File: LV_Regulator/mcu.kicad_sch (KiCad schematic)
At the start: 20 parts, among them U4 STM32F103C8Tx, Y1 32.768kHz, Y2 8MHz

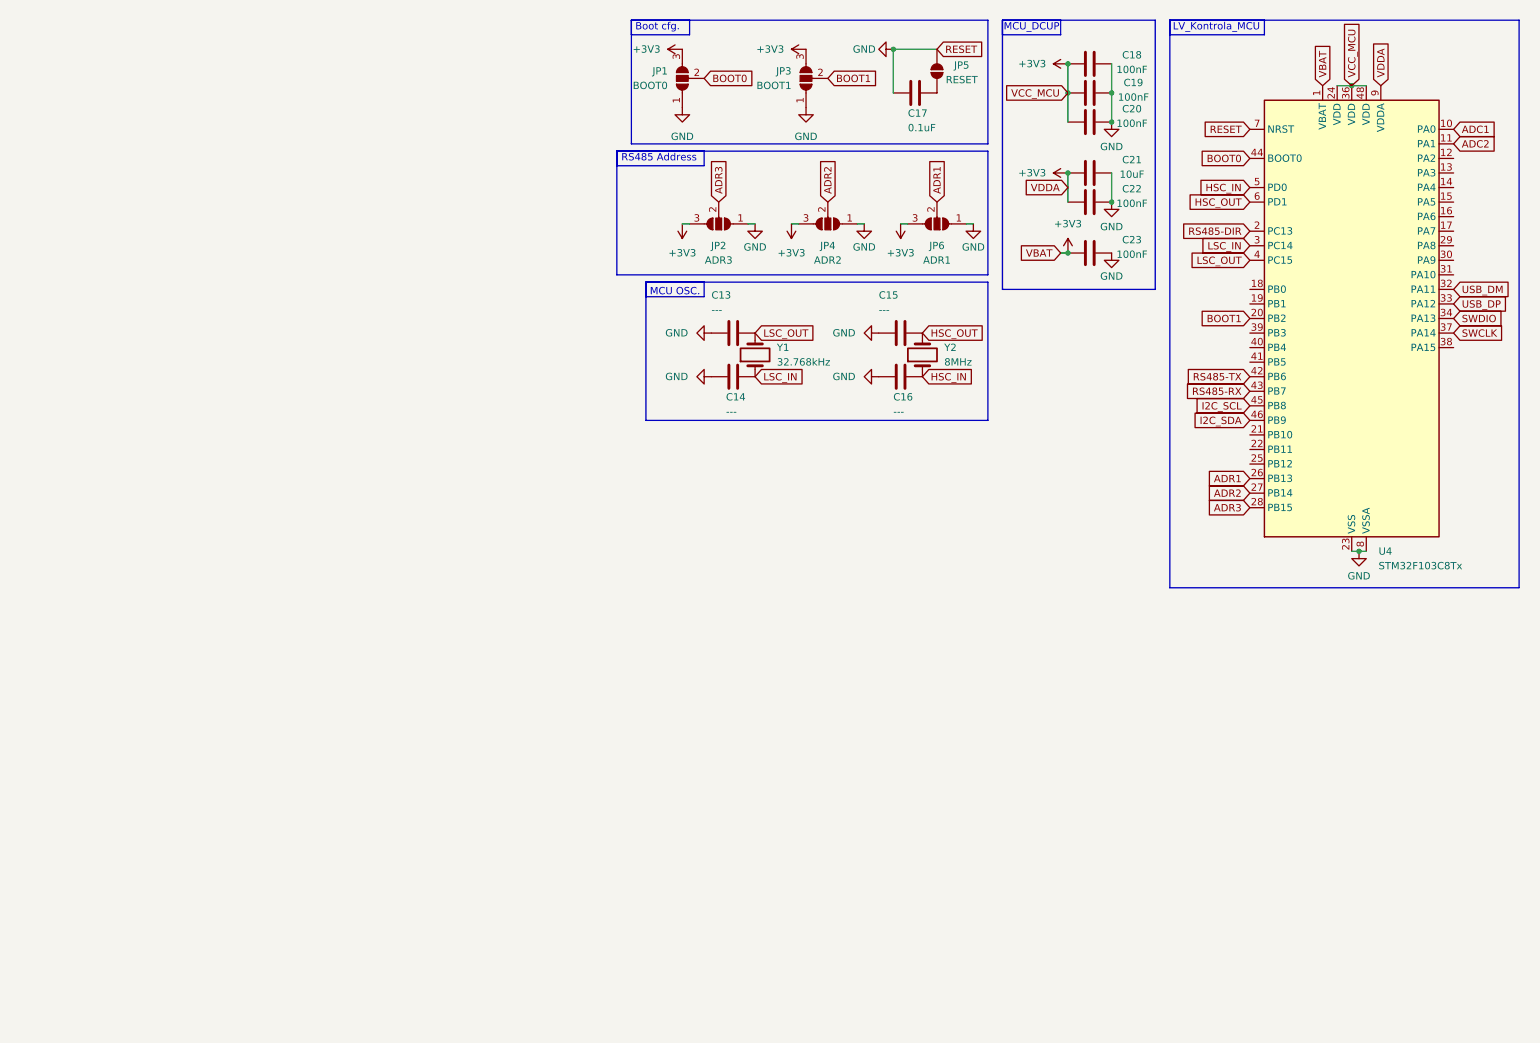
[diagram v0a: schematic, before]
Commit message: LV_Regulator Control changes
Added debug and development equipment, added config. eeprom, more...
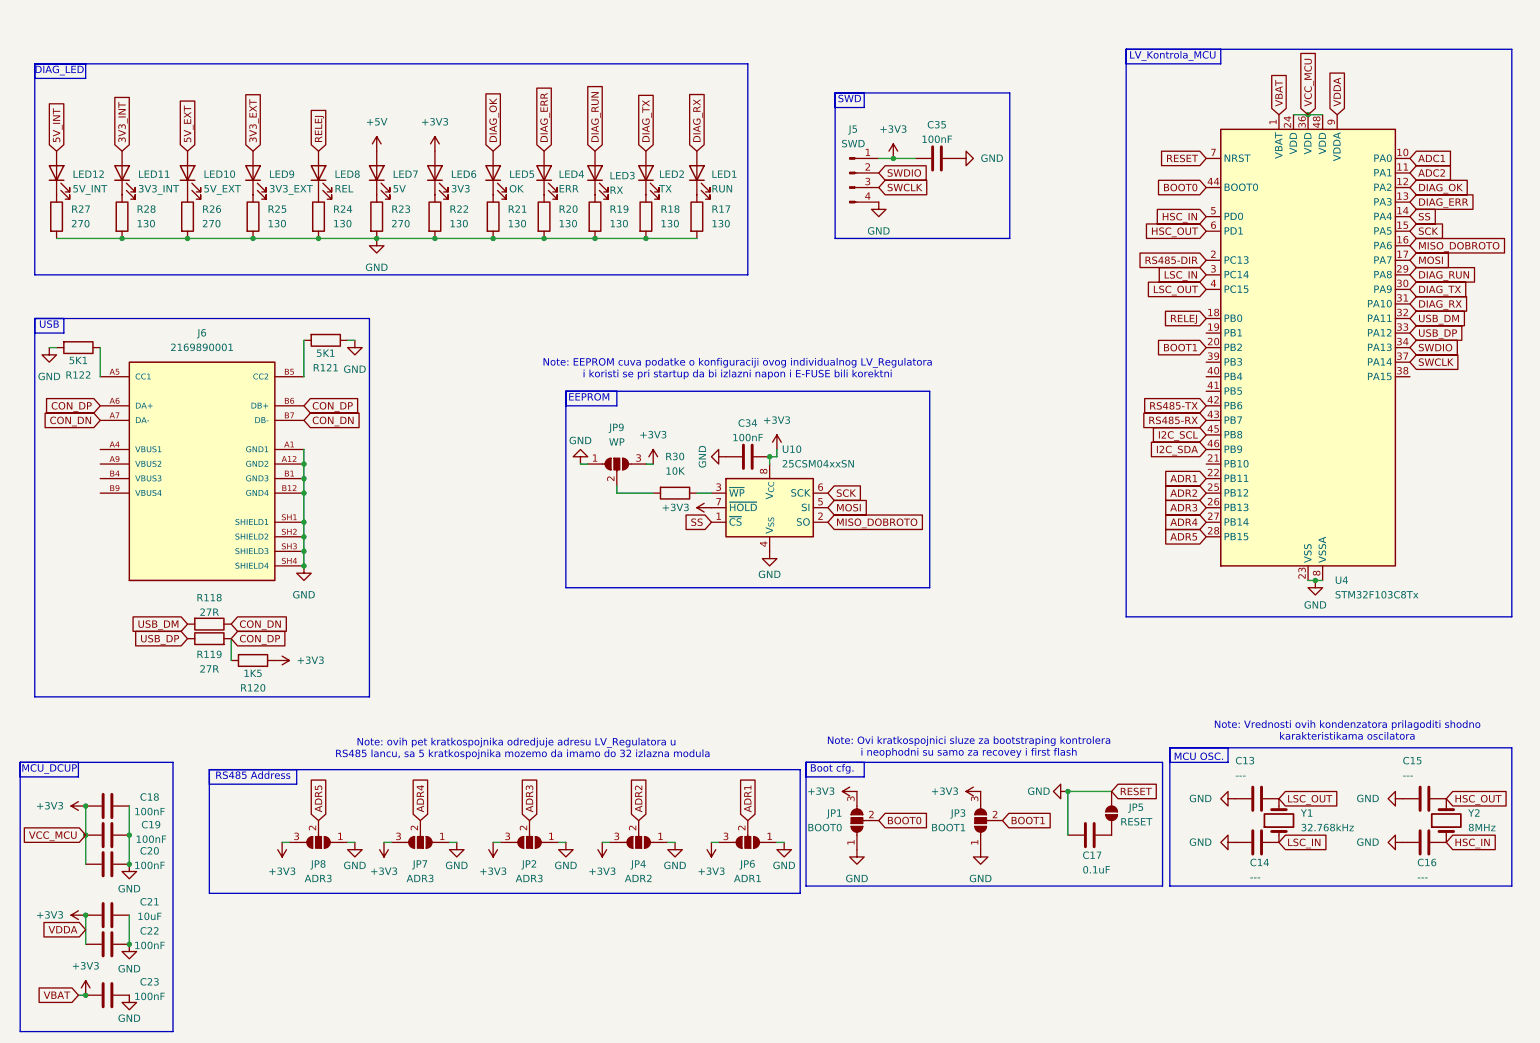
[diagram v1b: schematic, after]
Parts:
- added C34, C35: 100nF, symbol Device:C
- added J5: SWD, symbol Connector:Conn_01x04_Pin
- added J6: 2169890001, USB-C:MOLEX_2169890001, symbol 2169890001:2169890001
- added JP7, JP8: ADR3, symbol Jumper:SolderJumper_3_Open
- added JP9: WP, symbol Jumper:SolderJumper_3_Open
- added LED1: RUN, symbol Device:LED
- added LED10: 5V_EXT, symbol Device:LED
- added LED11: 3V3_INT, symbol Device:LED
- added LED12: 5V_INT, symbol Device:LED
- added LED2: TX, symbol Device:LED
- added LED3: RX, symbol Device:LED
- added LED4: ERR, symbol Device:LED
- added LED5: OK, symbol Device:LED
- added LED6: 3V3, symbol Device:LED
- added LED7: 5V, symbol Device:LED
- added LED8: REL, symbol Device:LED
- added LED9: 3V3_EXT, symbol Device:LED
- added R118, R119: 27R, Resistor_SMD:R_1206_3216Metric_Pad1.30x1.75mm_HandSolder, symbol Device:R
- added R120: 1K5, Resistor_SMD:R_1206_3216Metric_Pad1.30x1.75mm_HandSolder, symbol Device:R
- added R121, R122: 5K1, Resistor_SMD:R_1206_3216Metric_Pad1.30x1.75mm_HandSolder, symbol Device:R
- added R17, R18, R19, R20, R21, R22, R24, R25, R28: 130, symbol Device:R
- added R23, R26, R27: 270, symbol Device:R
- added R30: 10K, symbol Device:R
- added U10: 25CSM04xxSN, Package_SO:SOIC-8_3.9x4.9mm_P1.27mm, symbol Memory_EEPROM:25CSM04xxSN
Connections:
- net +3V3: now also C34.1, C35.2, J5.1 (Pin_1), JP7.3 (B), JP8.3 (B), JP9.3 (B), LED6.2 (A), R120.1, U10.7 (~{HOLD}), U10.8 (V_{CC})
- net ADR1: now also U4.22 (PB11); no longer U4.26 (PB13)
- net ADR2: now also U4.25 (PB12); no longer U4.27 (PB14)
- net ADR3: now also U4.26 (PB13); no longer U4.28 (PB15)
- net GND: now also C34.2, C35.1, J5.4 (Pin_4), J6.A1 (GND1), J6.A12 (GND2), J6.B1 (GND3), J6.B12 (GND4), J6.SH1 (SHIELD1), J6.SH2 (SHIELD2), J6.SH3 (SHIELD3), J6.SH4 (SHIELD4), JP7.1 (A), JP8.1 (A), JP9.1 (A), R121.1, R122.2, R17.2, R18.2, R19.2, R20.2, R21.2, R22.2, R23.2, R24.2, R25.2, R26.2, R27.2, R28.2, U10.4 (V_{SS})
- net SWCLK: now also J5.3 (Pin_3)
- net SWDIO: now also J5.2 (Pin_2)
- net USB_DM: now also R118.2
- net USB_DP: now also R119.1
- net DIAG_OK: now reaches U4.12 (PA2)
- net DIAG_OK: now also LED5.2 (A)
- net DIAG_ERR: now reaches U4.13 (PA3)
- net DIAG_ERR: now also LED4.2 (A)
- net SS: now reaches U4.14 (PA4)
- net SS: now also U10.1 (~{CS})
- net SCK: now reaches U4.15 (PA5)
- net SCK: now also U10.6 (SCK)
- net MISO_DOBROTO: now reaches U4.16 (PA6)
- net MISO_DOBROTO: now also U10.2 (SO)
- net MOSI: now reaches U4.17 (PA7)
- net MOSI: now also U10.5 (SI)
- net RELEJ: now reaches U4.18 (PB0)
- net RELEJ: now also LED8.2 (A)
- net DIAG_RUN: now reaches U4.29 (PA8)
- net DIAG_RUN: now also LED3.2 (A)
- net DIAG_TX: now reaches U4.30 (PA9)
- net DIAG_TX: now also LED2.2 (A)
- net DIAG_RX: now reaches U4.31 (PA10)
- net DIAG_RX: now also LED1.2 (A)
- new net: LED7.1 (K), R23.1
- new net: R30.1, U10.3 (~{WP})
- new net: J6.A5 (CC1), R122.1
- new net: J6.B5 (CC2), R121.2
- new net: LED6.1 (K), R22.1
- new net: LED2.1 (K), R18.1
- new net: JP9.2 (C), R30.2
- new net: LED12.1 (K), R27.1
- new net: LED4.1 (K), R20.1
- new net: LED9.1 (K), R25.1
- new net: LED11.1 (K), R28.1
- new net: LED1.1 (K), R17.1
- new net: LED5.1 (K), R21.1
- new net: LED10.1 (K), R26.1
- new net: LED3.1 (K), R19.1
- new net: LED8.1 (K), R24.1
- new net +5V: LED7.2 (A)
- new net 3V3_EXT: LED9.2 (A)
- new net 3V3_INT: LED11.2 (A)
- new net 5V_EXT: LED10.2 (A)
- new net 5V_INT: LED12.2 (A)
- new net ADR4: JP7.2 (C), U4.27 (PB14)
- new net ADR5: JP8.2 (C), U4.28 (PB15)
- new net CON_DN: J6.A7 (DA-), J6.B7 (DB-), R118.1
- new net CON_DP: J6.A6 (DA+), J6.B6 (DB+), R119.2, R120.2
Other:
- note added: "DIAG_LED"
- note added: "EEPROM"
- note added: "Note: EEPROM cuva podatke o konfiguraciji ovog individualnog LV_Regulatora i koristi se pri startup da bi izlazni napon i E-FUSE bili korektni"
- note added: "Note: Ovi kratkospojnici sluze za bootstraping kontrolera i neophodni su samo za recovey i first flash"
- note added: "Note: Vrednosti ovih kondenzatora prilagoditi shodno karakteristikama oscilatora"
- note added: "Note: ovih pet kratkospojnika odredjuje adresu LV_Regulatora u RS485 lancu, sa 5 kratkospojnika mozemo da imamo do 32 izlazna modula"
- note added: "SWD"
- note added: "USB"
- moved on the sheet: C13, C14, C15, C16, C17, C18, C19, C20, C21, C22, C23, JP1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

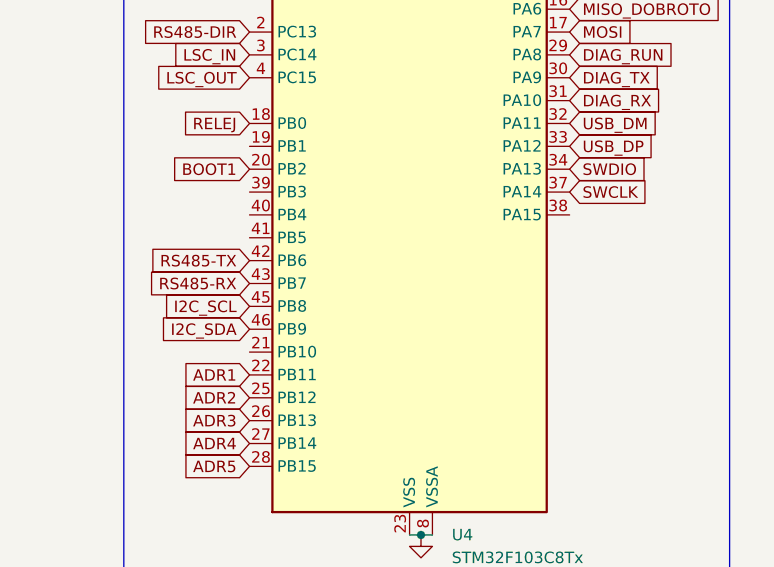
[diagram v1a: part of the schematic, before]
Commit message: Regulator Update & MCU pins
Update schematic and connected Regulator to MCU
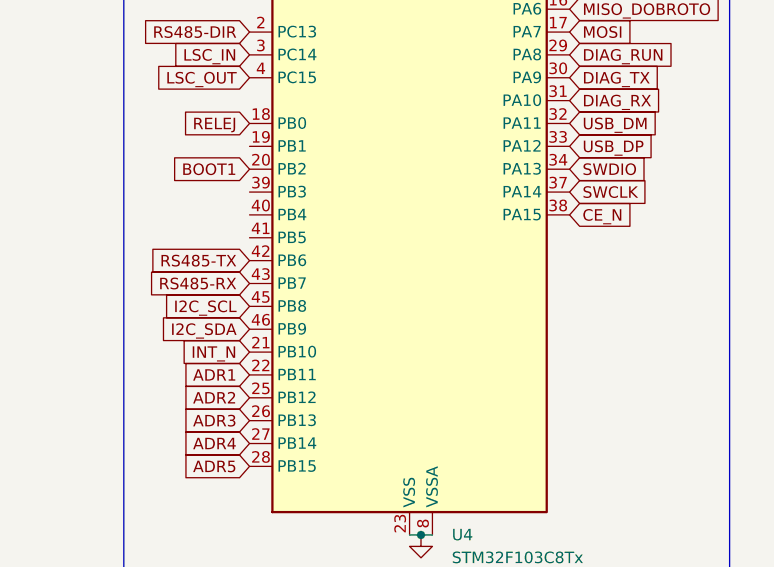
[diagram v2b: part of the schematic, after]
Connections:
- net INT_N: now reaches U4.21 (PB10)
- net CE_N: now reaches U4.38 (PA15)
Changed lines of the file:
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@@
+		)
+	)
+	(global_label "CE_N"
+		(shape input)
+		(at 264.16 76.2 0)
+		(fields_autoplaced yes)
+		(effects
+			(font
+				(size 1.27 1.27)
+			)
+			(justify left)
+		)
+		(property "Intersheetrefs" "${INTERSHEET_REFS}"
+			(at 271.8623 76.2 0)
+			(effects
+				(font
+					(size 1.27 1.27)
+				)
+				(justify left)
+				(hide yes)
+			)
 		)
 	)
@@
 			(effects
 				(font
+					(size 1.27 1.27)
+				)
+				(justify right)
+				(hide yes)
+			)
+		)
+	)
+	(global_label "INT_N"
+		(shape input)
+		(at 228.6 91.44 180)
+		(fields_autoplaced yes)
+		(effects
+			(font
+				(size 1.27 1.27)
+			)
+			(justify right)
+		)
+		(property "Intersheetrefs" "${INTERSHEET_REFS}"
+			(at 220.4138 91.44 0)
+			(effects
+				(font

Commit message: added certain footprints
Added footprints for certain parts such as the BQ25858Q1 regulator controller & CSD19506 MOSFET for PCB design and put in footprints (will need change)
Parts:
- C13, C14, C15, C16, C17, C18, C19, C20, C21, C22, C23: footprint (none) -> Capacitor_SMD:C_1206_3216Metric
- JP1, JP2, JP3, JP4, JP6, JP7, JP8: footprint (none) -> Jumper:SolderJumper-3_P1.3mm_Open_Pad1.0x1.5mm
- JP5: footprint (none) -> Jumper:SolderJumper-2_P1.3mm_Open_Pad1.0x1.5mm
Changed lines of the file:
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@@
 			)
 		)
-		(property "Footprint" ""
+		(property "Footprint" "Jumper:SolderJumper-3_P1.3mm_Open_Pad1.0x1.5mm"
 			(at 189.23 153.67 0)
 			(effects
@@
 			)
 		)
-		(property "Footprint" ""
+		(property "Footprint" "Jumper:SolderJumper-3_P1.3mm_Open_Pad1.0x1.5mm"
 			(at 167.64 153.67 0)
 			(effects
@@
 			)
 		)
-		(property "Footprint" ""
+		(property "Footprint" "Capacitor_SMD:C_1206_3216Metric"
 			(at 241.3 148.8948 0)
 			(effects
@@
 			)
 		)
-		(property "Footprint" ""
+		(property "Footprint" "Capacitor_SMD:C_1206_3216Metric"
 			(at 40.64 160.3248 0)
 			(effects
@@
 			)
 		)
-		(property "Footprint" ""
+		(property "Footprint" "Jumper:SolderJumper-3_P1.3mm_Open_Pad1.0x1.5mm"
 			(at 148.59 157.48 0)
 			(effects
@@
 			)
 		)
-		(property "Footprint" ""
+		(property "Footprint" "Capacitor_SMD:C_1206_3216Metric"
 			(at 40.64 169.2148 0)
 			(effects
@@
 			)
 		)
-		(property "Footprint" ""
+		(property "Footprint" "Capacitor_SMD:C_1206_3216Metric"
 			(at 40.64 150.1648 0)
 			(effects
@@
 			)
 		)
-		(property "Footprint" ""
+		(property "Footprint" "Jumper:SolderJumper-3_P1.3mm_Open_Pad1.0x1.5mm"
 			(at 91.44 157.48 0)
 			(effects
@@
 			)
 		)
-		(property "Footprint" ""
+		(property "Footprint" "Capacitor_SMD:C_1206_3216Metric"
 			(at 40.64 155.2448 0)
 			(effects
@@
 			)
 		)
-		(property "Footprint" ""
+		(property "Footprint" "Jumper:SolderJumper-3_P1.3mm_Open_Pad1.0x1.5mm"
 			(at 73.66 157.48 0)
 			(effects
@@
 			)
 		)
-		(property "Footprint" ""
+		(property "Footprint" "Capacitor_SMD:C_1206_3216Metric"
 			(at 40.64 174.2948 0)
 			(effects
@@
 			)
 		)
-		(property "Footprint" ""
+		(property "Footprint" "Capacitor_SMD:C_1206_3216Metric"
 			(at 262.89 158.4452 0)
 			(effects
@@
 			)
 		)
-		(property "Footprint" ""
+		(property "Footprint" "Jumper:SolderJumper-2_P1.3mm_Open_Pad1.0x1.5mm"
 			(at 212.09 152.4 0)
 			(effects
@@
 			)
 		)
-		(property "Footprint" ""
+		(property "Footprint" "Capacitor_SMD:C_1206_3216Metric"
 			(at 233.68 158.4452 0)
 			(effects
@@
 			)
 		)
-		(property "Footprint" ""
+		(property "Footprint" "Jumper:SolderJumper-3_P1.3mm_Open_Pad1.0x1.5mm"
 			(at 110.49 157.48 0)
 			(effects
@@
 			)
 		)
-		(property "Footprint" ""
+		(property "Footprint" "Capacitor_SMD:C_1206_3216Metric"
 			(at 204.47 157.1752 0)
 			(effects
@@
 			)
 		)
-		(property "Footprint" ""
+		(property "Footprint" "Jumper:SolderJumper-3_P1.3mm_Open_Pad1.0x1.5mm"
 			(at 129.54 157.48 0)
 			(effects
@@
 			)
 		)
-		(property "Footprint" ""
+		(property "Footprint" "Capacitor_SMD:C_1206_3216Metric"
 			(at 270.51 148.8948 0)
 			(effects
@@
 			)
 		)
-		(property "Footprint" ""
+		(property "Footprint" "Capacitor_SMD:C_1206_3216Metric"
 			(at 40.64 183.1848 0)
 			(effects

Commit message: Multiple Footprints Added
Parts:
- J6: footprint USB-C:MOLEX_2169890001 -> USB_C:MOLEX_2169890001
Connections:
- no-connect marks 0 -> 8
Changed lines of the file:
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@@
 		(color 0 0 0 0)
+	)
+	(no_connect
+		(at 228.6 78.74)
+	)
+	(no_connect
+		(at 228.6 76.2)
+	)
+	(no_connect
+		(at 35.56 91.44)
+	)
+	(no_connect
+		(at 35.56 96.52)
+	)
+	(no_connect
+		(at 35.56 93.98)
+	)
+	(no_connect
+		(at 35.56 88.9)
+	)
+	(no_connect
+		(at 228.6 68.58)
+	)
+	(no_connect
+		(at 228.6 73.66)
 	)
 	(wire
@@
 			)
 		)
-		(property "Footprint" "USB-C:MOLEX_2169890001"
+		(property "Footprint" "USB_C:MOLEX_2169890001"
 			(at 53.34 91.44 0)
 			(effects

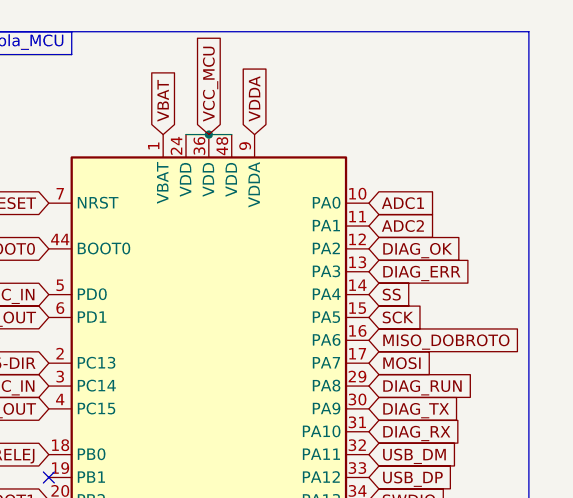
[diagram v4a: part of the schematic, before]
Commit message: Update to LV_Regulator schematic
Chosen some component's footprints as well as made a page for test points, etc.
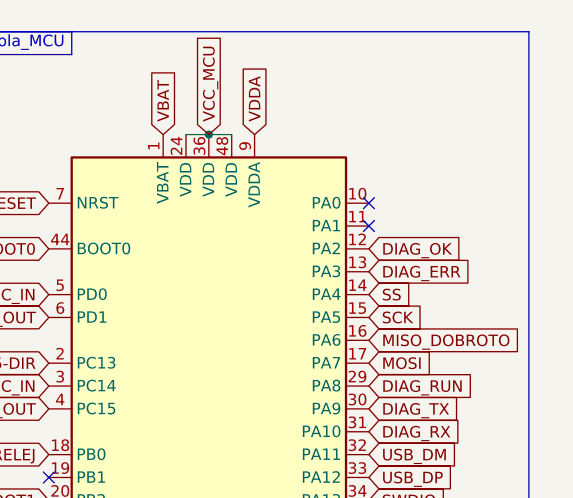
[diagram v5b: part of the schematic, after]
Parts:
- J5: footprint (none) -> Connector_PinHeader_1.00mm:PinHeader_1x04_P1.00mm_Vertical
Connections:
- net ADC1: no longer names the net of U4.10 (PA0)
- net ADC2: no longer names the net of U4.11 (PA1)
- no-connect marks 8 -> 10
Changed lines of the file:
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@@
 	)
 	(no_connect
+		(at 264.16 40.64)
+	)
+	(no_connect
 		(at 228.6 76.2)
 	)
 	(no_connect
+		(at 264.16 38.1)
+	)
+	(no_connect
 		(at 35.56 91.44)
 	)
@@
 		)
 	)
-	(global_label "ADC1"
-		(shape input)
-		(at 264.16 38.1 0)
-		(fields_autoplaced yes)
-		(effects
-			(font
-				(size 1.27 1.27)
-			)
-			(justify left)
-		)
-		(property "Intersheetrefs" "${INTERSHEET_REFS}"
-			(at 271.9833 38.1 0)
-			(effects
-				(font
-					(size 1.27 1.27)
-				)
-				(justify left)
-				(hide yes)
-			)
-		)
-	)
 	(global_label "SWDIO"
 		(shape input)
@@
 		)
 	)
-	(global_label "ADC2"
-		(shape input)
-		(at 264.16 40.64 0)
-		(fields_autoplaced yes)
-		(effects
-			(font
-				(size 1.27 1.27)
-			)
-			(justify left)
-		)
-		(property "Intersheetrefs" "${INTERSHEET_REFS}"
-			(at 271.9833 40.64 0)
-			(effects
-				(font
-					(size 1.27 1.27)
-				)
-				(justify left)
-				(hide yes)
-			)
-		)
-	)
 	(global_label "ADR5"
 		(shape input)
@@
 			)
 		)
-		(property "Footprint" ""
+		(property "Footprint" "Connector_PinHeader_1.00mm:PinHeader_1x04_P1.00mm_Vertical"
 			(at 166.37 40.64 0)
 			(effects
